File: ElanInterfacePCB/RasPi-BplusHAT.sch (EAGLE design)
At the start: 7 parts, among them J1 RASPBERRYPI-40-PIN-GPIO_PTH_N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, Q1 310mA/60V/1.6Ω, Q2 1.1A/60V/600mΩ

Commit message: PCB Work
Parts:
- removed C1: (no value), rcl:C-USC0805
- removed J1: RASPBERRYPI-40-PIN-GPIO_PTH_NO_SHROUD, SparkFun-Connectors:RASPBERRYPI-40-PIN-GPIO_PTH_NO_SHROUD
- added C2, C3: (no value), rcl:C-USC0805
- added D2, D3, D4, D5, D6: BAS40-04, diode:BAS40-04
- added K1: PIN20X2, FLYFISH:PIN20X2
- added Q10, Q12, Q4, Q6, Q8: 1.1A/60V/600mΩ, SparkFun-DiscreteSemi:MOSFET_PCH-SI2309DS
- added Q11, Q3, Q5, Q7, Q9: 310mA/60V/1.6Ω, SparkFun-DiscreteSemi:MOSFET-NCH-2N7002PW
- added R10, R12, R5, R6, R8: 1k, resistor:R-US_R0805
- added R11, R3, R4, R7, R9: 100, resistor:R-US_R0805
- added U2: MAX481CUA+, MAX481CUA_:MAX481CUA+
- R1: value (none) -> 100
- R2: value (none) -> 1k
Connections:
- new net +3V3: C3.1, K1.1, K1.17, U2.VCC
- new net +5V: K1.2, K1.4
- new net N$10: D5.C1A2, Q10.S, R9.1
- new net N$11: Q11.D, Q12.G, R12.1
- new net N$12: D6.C1A2, Q12.S, R11.1
- new net N$3: Q5.D, Q6.G, R6.1
- new net N$5: D1.C1A2, Q2.S, R4.1
- new net N$6: D3.C1A2, Q6.S, R3.1
- new net N$7: Q7.D, Q8.G, R8.1
- new net N$8: D4.C1A2, Q8.S, R7.1
- new net N$9: Q10.G, Q9.D, R10.1
- new net RXI: K1.10, U2.RO
- new net ZONE1: R1.2, R11.2, R3.2, R4.2, R7.2, R9.2
- net +12V: now also C2.1, D2.C2, D3.C2, D4.C2, D5.C2, D6.C2, Q10.D, Q12.D, Q4.D, Q6.D, Q8.D, R10.2, R12.2, R5.2, R6.2, R8.2; no longer C1.1
- net GND: now also C2.2, C3.2, D2.A1, D3.A1, D4.A1, D5.A1, D6.A1, K1.14, K1.20, K1.25, K1.30, K1.34, K1.39, K1.6, K1.9, Q11.S, Q3.S, Q5.S, Q7.S, Q9.S, U2.DE, U2.GND, U2.~RE; no longer C1.2, J1.GND@14, J1.GND@20, J1.GND@25, J1.GND@30, J1.GND@34, J1.GND@39, J1.GND@6, J1.GND@9
- net GPIO07: now also K1.26, Q1.G, Q11.G; no longer J1.CE1
- net GPIO08: now also K1.24, Q3.G; no longer J1.CE0
- net GPIO09: now also K1.21, Q5.G; no longer J1.MISO
- net GPIO10: now also K1.19, Q7.G; no longer J1.MOSI
- net GPIO11: now also K1.23, Q9.G; no longer J1.SCLK
- net N$1: now also Q3.D, Q4.G, R2.1; no longer Q1.G
- net N$2: now also D2.C1A2, Q4.S, R1.1; no longer Q1.D, Q2.G, R2.1
- net N$4: now also Q1.D, Q2.G, R5.1; no longer D1.C1A2, Q2.S, R1.1
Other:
- note added: "Checked by:"
- note added: "Drawn by:"
- note added: "FLYFISH TECHNOLOGIES d.o.o."
- note added: "Ivan Zilic"
- note added: "v0.1"
- moved on the sheet: D1, Q1, Q2, R1, R2

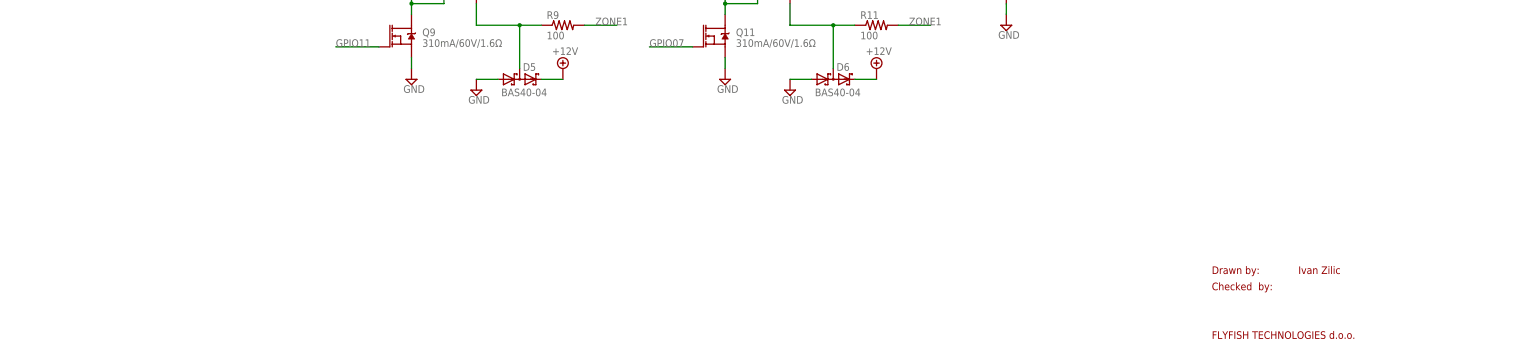
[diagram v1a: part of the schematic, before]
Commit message: Fix pin numberbing on rj45
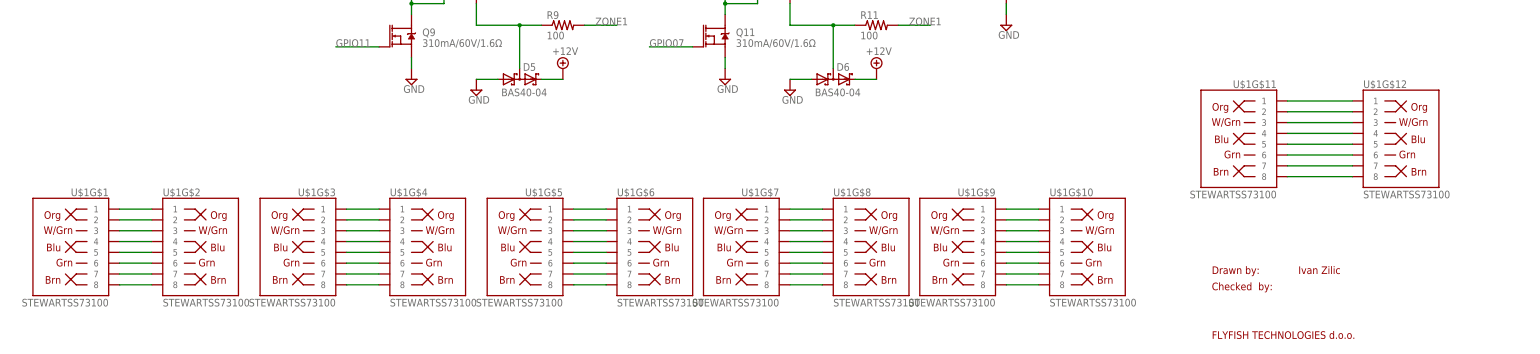
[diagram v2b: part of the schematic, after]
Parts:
- added U$1: STEWARTSS73100, Stewart_Connector_SS73100-046F:STEWARTSS73100
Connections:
- new net N$13: U$1G$1.8, U$1G$2.8
- new net N$14: U$1G$1.7, U$1G$2.7
- new net N$15: U$1G$1.6, U$1G$2.6
- new net N$16: U$1G$1.5, U$1G$2.5
- new net N$17: U$1G$1.4, U$1G$2.4
- new net N$18: U$1G$1.3, U$1G$2.3
- new net N$19: U$1G$1.2, U$1G$2.2
- new net N$20: U$1G$1.1, U$1G$2.1
- new net N$21: U$1G$3.1, U$1G$4.1
- new net N$22: U$1G$3.2, U$1G$4.2
- new net N$23: U$1G$3.3, U$1G$4.3
- new net N$24: U$1G$3.4, U$1G$4.4
- new net N$25: U$1G$3.5, U$1G$4.5
- new net N$26: U$1G$3.7, U$1G$4.7
- new net N$27: U$1G$3.6, U$1G$4.6
- new net N$28: U$1G$3.8, U$1G$4.8
- new net N$29: U$1G$5.1, U$1G$6.1
- new net N$30: U$1G$5.2, U$1G$6.2
- new net N$31: U$1G$5.3, U$1G$6.3
- new net N$32: U$1G$5.4, U$1G$6.4
- new net N$33: U$1G$5.5, U$1G$6.5
- new net N$34: U$1G$5.6, U$1G$6.6
- new net N$35: U$1G$5.7, U$1G$6.7
- new net N$36: U$1G$5.8, U$1G$6.8
- new net N$37: U$1G$7.1, U$1G$8.1
- new net N$38: U$1G$7.2, U$1G$8.2
- new net N$39: U$1G$7.3, U$1G$8.3
- new net N$40: U$1G$7.4, U$1G$8.4
- new net N$41: U$1G$7.5, U$1G$8.5
- new net N$42: U$1G$7.6, U$1G$8.6
- new net N$43: U$1G$7.7, U$1G$8.7
- new net N$44: U$1G$7.8, U$1G$8.8
- new net N$45: U$1G$10.1, U$1G$9.1
- new net N$46: U$1G$10.2, U$1G$9.2
- new net N$47: U$1G$10.3, U$1G$9.3
- new net N$48: U$1G$10.4, U$1G$9.4
- new net N$49: U$1G$10.5, U$1G$9.5
- new net N$50: U$1G$10.6, U$1G$9.6
- new net N$51: U$1G$10.7, U$1G$9.7
- new net N$52: U$1G$10.8, U$1G$9.8
- new net N$53: U$1G$11.1, U$1G$12.1
- new net N$54: U$1G$11.2, U$1G$12.2
- new net N$55: U$1G$11.3, U$1G$12.3
- new net N$56: U$1G$11.4, U$1G$12.4
- new net N$57: U$1G$11.5, U$1G$12.5
- new net N$58: U$1G$11.6, U$1G$12.6
- new net N$59: U$1G$11.7, U$1G$12.7
- new net N$60: U$1G$11.8, U$1G$12.8

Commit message: PCB Update
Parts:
- removed Q11: 310mA/60V/1.6Ω, SparkFun-DiscreteSemi:MOSFET-NCH-2N7002PW
- added C1, C4, C5, C6, C7: (no value), rcl:C-USC0805
- added JP1: (no value), pinhead:PINHD-2X4
- added Q13: 220mA/50V/3.5Ω, SparkFun-DiscreteSemi:MOSFET-NCH-BSS138
- Q1, Q3, Q5, Q7, Q9: value 310mA/60V/1.6Ω -> 220mA/50V/3.5Ω; device SparkFun-DiscreteSemi:MOSFET-NCH-2N7002PW -> SparkFun-DiscreteSemi:MOSFET-NCH-BSS138
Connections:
- removed net N$14: U$1G$1.7, U$1G$2.7
- removed net N$15 (its old number): U$1G$1.6, U$1G$2.6
- removed net N$16: U$1G$1.5, U$1G$2.5
- removed net N$17: U$1G$1.4, U$1G$2.4
- removed net N$19: U$1G$1.2, U$1G$2.2
- removed net N$22: U$1G$3.2, U$1G$4.2
- removed net N$26: U$1G$3.7, U$1G$4.7
- removed net N$27: U$1G$3.6, U$1G$4.6
- removed net N$30: U$1G$5.2, U$1G$6.2
- removed net N$34: U$1G$5.6, U$1G$6.6
- removed net N$35: U$1G$5.7, U$1G$6.7
- removed net N$38: U$1G$7.2, U$1G$8.2
- removed net N$42: U$1G$7.6, U$1G$8.6
- removed net N$43: U$1G$7.7, U$1G$8.7
- removed net N$46: U$1G$10.2, U$1G$9.2
- removed net N$50: U$1G$10.6, U$1G$9.6
- removed net N$51: U$1G$10.7, U$1G$9.7
- removed net N$54: U$1G$11.2, U$1G$12.2
- removed net N$58: U$1G$11.6, U$1G$12.6
- removed net N$59: U$1G$11.7, U$1G$12.7
- new net 485+: U$1G$1.4, U$1G$2.4, U2.A
- new net 485-: U$1G$1.5, U$1G$2.5, U2.B
- new net GPIO02: JP1.2, K1.3
- new net GPIO06: JP1.4, K1.31
- new net GPIO12: JP1.6, K1.32
- new net GPIO21: JP1.8, K1.40
- new net GPIOSEL: JP1.1, JP1.3, JP1.5, JP1.7, Q9.G
- new net ZONE2: R1.2, U$1G$3.2, U$1G$4.2
- new net ZONE3: R3.2, U$1G$5.2, U$1G$6.2
- new net ZONE4: R7.2, U$1G$7.2, U$1G$8.2
- new net ZONE5: R9.2, U$1G$10.2, U$1G$9.2
- new net ZONE6: R11.2, U$1G$11.2, U$1G$12.2
- net +12V: now also C1.1, C4.1, C5.1, C6.1, C7.1, U$1G$1.6, U$1G$10.6, U$1G$11.6, U$1G$12.6, U$1G$2.6, U$1G$3.6, U$1G$4.6, U$1G$5.6, U$1G$6.6, U$1G$7.6, U$1G$8.6, U$1G$9.6
- net +3V3: no longer K1.17
- net GND: now also C1.2, C4.2, C5.2, C6.2, C7.2, Q13.S, U$1G$1.7, U$1G$10.7, U$1G$11.7, U$1G$12.7, U$1G$2.7, U$1G$3.7, U$1G$4.7, U$1G$5.7, U$1G$6.7, U$1G$7.7, U$1G$8.7, U$1G$9.7; no longer Q11.S
- net GPIO07: now also Q13.G; no longer Q1.G, Q11.G
- net GPIO08: now also Q1.G; no longer Q3.G
- net GPIO09: now also Q3.G; no longer Q5.G
- net GPIO10: now also Q5.G; no longer Q7.G
- net GPIO11: now also Q7.G; no longer Q9.G
- net N$1: now also Q1.D; no longer Q3.D
- net N$11: now also Q9.D; no longer Q11.D
- net N$3: now also Q3.D; no longer Q5.D
- net N$4: now also Q13.D; no longer Q1.D
- net N$7: now also Q5.D; no longer Q7.D
- net N$9: now also Q7.D; no longer Q9.D
- net ZONE1: now also U$1G$1.2, U$1G$2.2; no longer R1.2, R11.2, R3.2, R7.2, R9.2
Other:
- note added: "Jeremy Rode"
- note removed: "Ivan Zilic"
- moved on the sheet: Q1, Q3, Q5, Q7, Q9, U$1G$10, U$1G$2, U$1G$3, U$1G$4, U$1G$5, U$1G$6, U$1G$7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

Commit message: Finished PCB
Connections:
- removed net +5V: K1.2, K1.4
- new net N$17: U2.DI
- net ZONE1: now also R7.2; no longer R4.2
- net ZONE2: now also R3.2; no longer R1.2
- net ZONE3: now also R9.2; no longer R3.2
- net ZONE4: now also R1.2; no longer R7.2
- net ZONE5: now also R4.2; no longer R9.2
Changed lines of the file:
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@@
 <part name="+3V1" library="supply1" library_urn="urn:adsk.eagle:library:371" deviceset="+3V3" device=""/>
 <part name="GND3" library="supply1" library_urn="urn:adsk.eagle:library:371" deviceset="GND" device=""/>
-<part name="P+1" library="supply1" library_urn="urn:adsk.eagle:library:371" deviceset="+5V" device=""/>
 <part name="Q2" library="SparkFun-DiscreteSemi" library_urn="urn:adsk.eagle:library:514" deviceset="MOSFET_PCH" device="-SI2309DS" package3d_urn="urn:adsk.eagle:package:38446/1" value="1.1A/60V/600mΩ"/>
 <part name="R4" library="resistor" library_urn="urn:adsk.eagle:library:348" deviceset="R-US_" device="R0805" package3d_urn="urn:adsk.eagle:package:26059/1" value="100"/>
@@
 <part name="SUPPLY9" library="supply2" library_urn="urn:adsk.eagle:library:372" deviceset="GND" device=""/>
 <part name="+3V2" library="supply1" library_urn="urn:adsk.eagle:library:371" deviceset="+3V3" device=""/>
-<part name="+3V3" library="supply1" library_urn="urn:adsk.eagle:library:371" deviceset="+3V3" device=""/>
 <part name="+3V4" library="supply1" library_urn="urn:adsk.eagle:library:371" deviceset="+3V3" device=""/>
 <part name="Q4" library="SparkFun-DiscreteSemi" library_urn="urn:adsk.eagle:library:514" deviceset="MOSFET_PCH" device="-SI2309DS" package3d_urn="urn:adsk.eagle:package:38446/1" value="1.1A/60V/600mΩ"/>
@@
 <part name="SUPPLY43" library="supply2" library_urn="urn:adsk.eagle:library:372" deviceset="GND" device=""/>
 <part name="SUPPLY44" library="supply2" library_urn="urn:adsk.eagle:library:372" deviceset="GND" device=""/>
-<part name="SUPPLY45" library="supply2" library_urn="urn:adsk.eagle:library:372" deviceset="+12V" device=""/>
 <part name="SUPPLY46" library="supply2" library_urn="urn:adsk.eagle:library:372" deviceset="+12V" device=""/>
 <part name="SUPPLY47" library="supply2" library_urn="urn:adsk.eagle:library:372" deviceset="+12V" device=""/>
@@
 </instance>
 <instance part="GND3" gate="1" x="40.64" y="121.92"/>
-<instance part="P+1" gate="1" x="60.96" y="182.88" smashed="yes">
-<attribute name="VALUE" x="63.5" y="185.42" size="1.778" layer="96" rot="R180"/>
-</instance>
 <instance part="Q2" gate="G$1" x="111.76" y="149.86"/>
 <instance part="R4" gate="G$1" x="134.62" y="139.7"/>
@@
 <instance part="SUPPLY9" gate="GND" x="170.18" y="200.66"/>
 <instance part="+3V2" gate="G$1" x="215.9" y="228.6" smashed="yes">
-<attribute name="VALUE" x="218.44" y="231.14" size="1.778" layer="96" rot="R180"/>
-</instance>
-<instance part="+3V3" gate="G$1" x="215.9" y="228.6" smashed="yes">
 <attribute name="VALUE" x="218.44" y="231.14" size="1.778" layer="96" rot="R180"/>
 </instance>
@@
 <instance part="SUPPLY43" gate="GND" x="259.08" y="10.16"/>
 <instance part="SUPPLY44" gate="GND" x="314.96" y="35.56"/>
-<instance part="SUPPLY45" gate="+12V" x="109.22" y="104.14"/>
 <instance part="SUPPLY46" gate="+12V" x="35.56" y="53.34"/>
 <instance part="SUPPLY47" gate="+12V" x="101.6" y="50.8"/>
@@
 <segment>
 <pinref part="+3V2" gate="G$1" pin="+3V3"/>
-<pinref part="+3V3" gate="G$1" pin="+3V3"/>
-<wire x1="215.9" y1="226.06" x2="215.9" y2="218.44" width="0.1524" layer="91"/>
-<junction x="215.9" y="226.06"/>
 <pinref part="U2" gate="A" pin="VCC"/>
-<wire x1="215.9" y1="218.44" x2="218.44" y2="218.44" width="0.1524" layer="91"/>
+<wire x1="218.44" y1="218.44" x2="215.9" y2="218.44" width="0.1524" layer="91"/>
+<wire x1="215.9" y1="218.44" x2="215.9" y2="226.06" width="0.1524" layer="91"/>
 </segment>
 <segment>
@@
 <wire x1="170.18" y1="213.36" x2="170.18" y2="220.98" width="0.1524" layer="91"/>
 <pinref part="+3V4" gate="G$1" pin="+3V3"/>
-</segment>
-</net>
-<net name="+5V" class="0">
-<segment>
-<pinref part="K1" gate="G$1" pin="2"/>
-<pinref part="P+1" gate="1" pin="+5V"/>
-<wire x1="58.42" y1="175.26" x2="60.96" y2="175.26" width="0.1524" layer="91"/>
-<wire x1="60.96" y1="175.26" x2="60.96" y2="180.34" width="0.1524" layer="91"/>
-<pinref part="K1" gate="G$1" pin="4"/>
-<wire x1="58.42" y1="172.72" x2="60.96" y2="172.72" width="0.1524" layer="91"/>
-<wire x1="60.96" y1="172.72" x2="60.96" y2="175.26" width="0.1524" layer="91"/>
-<junction x="60.96" y="175.26"/>
 </segment>
 </net>
@@
 <wire x1="116.84" y1="101.6" x2="116.84" y2="93.98" width="0.1524" layer="91"/>
 <junction x="109.22" y="101.6"/>
-<pinref part="SUPPLY45" gate="+12V" pin="+12V"/>
 </segment>
 <segment>
@@
 <net name="ZONE1" class="0">
 <segment>
-<pinref part="R4" gate="G$1" pin="2"/>
-<wire x1="139.7" y1="139.7" x2="147.32" y2="139.7" width="0.1524" layer="91"/>
-<label x="142.24" y="139.7" size="1.778" layer="95"/>
-</segment>
-<segment>
 <pinref part="U$1" gate="G$2" pin="2"/>
 <pinref part="U$1" gate="G$1" pin="2"/>
 <wire x1="50.8" y1="33.02" x2="33.02" y2="33.02" width="0.1524" layer="91"/>
 <label x="38.1" y="33.02" size="1.778" layer="95"/>
+</segment>
+<segment>
+<pinref part="R7" gate="G$1" pin="2"/>
+<wire x1="360.68" y1="137.16" x2="368.3" y2="137.16" width="0.1524" layer="91"/>
+<label x="363.22" y="137.16" size="1.778" layer="95"/>
 </segment>
 </net>
@@
 <net name="ZONE2" class="0">
 <segment>
-<pinref part="R1" gate="G$1" pin="2"/>
-<wire x1="213.36" y1="139.7" x2="220.98" y2="139.7" width="0.1524" layer="91"/>
-<label x="215.9" y="139.7" size="1.778" layer="95"/>
-</segment>
-<segment>
 <pinref part="U$1" gate="G$4" pin="2"/>
 <pinref part="U$1" gate="G$3" pin="2"/>
@@
 <label x="106.68" y="43.18" size="1.778" layer="95"/>
 </segment>
-</net>
-<net name="ZONE3" class="0">
 <segment>
 <pinref part="R3" gate="G$1" pin="2"/>
@@
 <label x="289.56" y="137.16" size="1.778" layer="95"/>
 </segment>
+</net>
+<net name="ZONE3" class="0">
 <segment>
 <pinref part="U$1" gate="G$5" pin="2"/>
@@
 <label x="160.02" y="45.72" size="1.778" layer="95"/>
 </segment>
+<segment>
+<pinref part="R9" gate="G$1" pin="2"/>
+<wire x1="142.24" y1="78.74" x2="149.86" y2="78.74" width="0.1524" layer="91"/>
+<label x="144.78" y="78.74" size="1.778" layer="95"/>
+</segment>
 </net>
 <net name="ZONE4" class="0">
-<segment>
-<pinref part="R7" gate="G$1" pin="2"/>
-<wire x1="360.68" y1="137.16" x2="368.3" y2="137.16" width="0.1524" layer="91"/>
-<label x="363.22" y="137.16" size="1.778" layer="95"/>
-</segment>
 <segment>
 <pinref part="U$1" gate="G$7" pin="2"/>
@@
 <label x="210.82" y="43.18" size="1.778" layer="95"/>
 </segment>
+<segment>
+<pinref part="R1" gate="G$1" pin="2"/>
+<wire x1="213.36" y1="139.7" x2="220.98" y2="139.7" width="0.1524" layer="91"/>
+<label x="215.9" y="139.7" size="1.778" layer="95"/>
+</segment>
 </net>
 <net name="ZONE5" class="0">
-<segment>
-<pinref part="R9" gate="G$1" pin="2"/>
-<wire x1="142.24" y1="78.74" x2="149.86" y2="78.74" width="0.1524" layer="91"/>
-<label x="144.78" y="78.74" size="1.778" layer="95"/>
-</segment>
 <segment>
 <pinref part="U$1" gate="G$10" pin="2"/>
@@
 <wire x1="259.08" y1="43.18" x2="271.78" y2="43.18" width="0.1524" layer="91"/>
 <label x="261.62" y="43.18" size="1.778" layer="95"/>
+</segment>
+<segment>
+<pinref part="R4" gate="G$1" pin="2"/>
+<wire x1="139.7" y1="139.7" x2="147.32" y2="139.7" width="0.1524" layer="91"/>
+<label x="142.24" y="139.7" size="1.778" layer="95"/>
 </segment>
 </net>
@@
 </segment>
 </net>
+<net name="N$17" class="0">
+<segment>
+<pinref part="U2" gate="A" pin="DI"/>
+<junction x="218.44" y="205.74"/>
+</segment>
+</net>
 </nets>
 </sheet>
 </sheets>
+<errors>
+</errors>
 </schematic>
 </drawing>

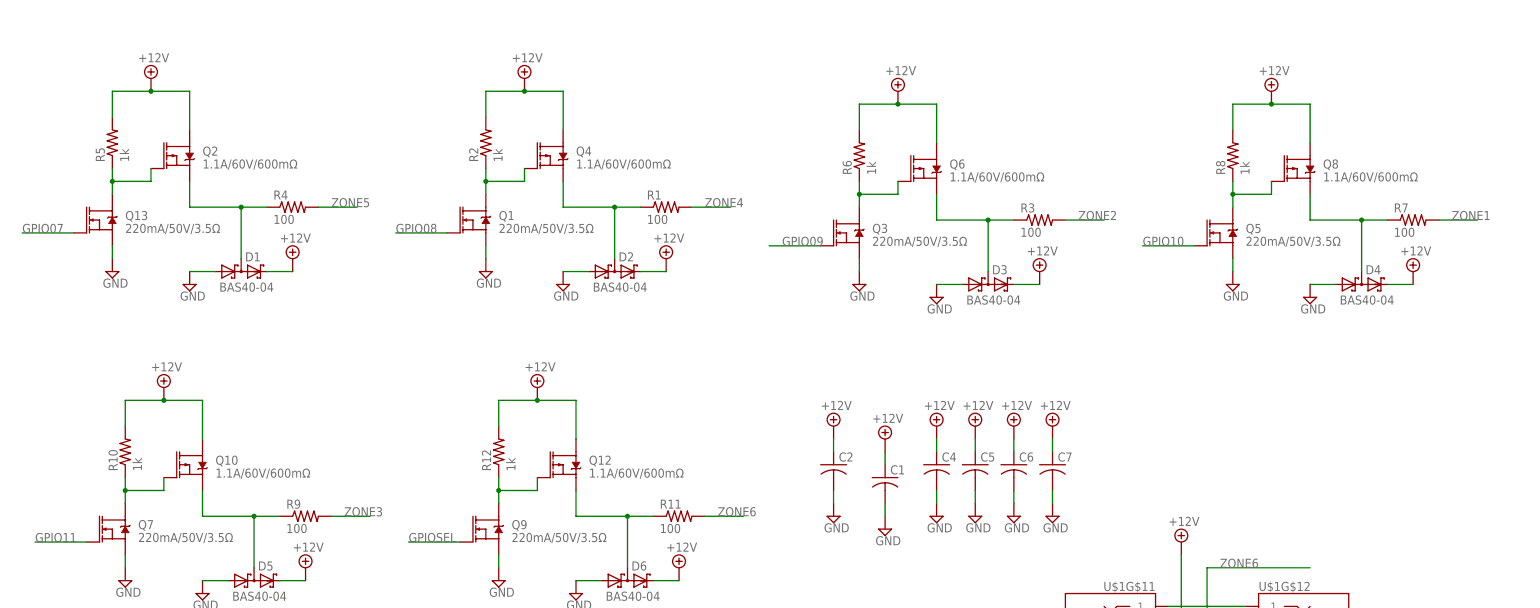
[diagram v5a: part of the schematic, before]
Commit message: Fixed inverted PMOS in schematic
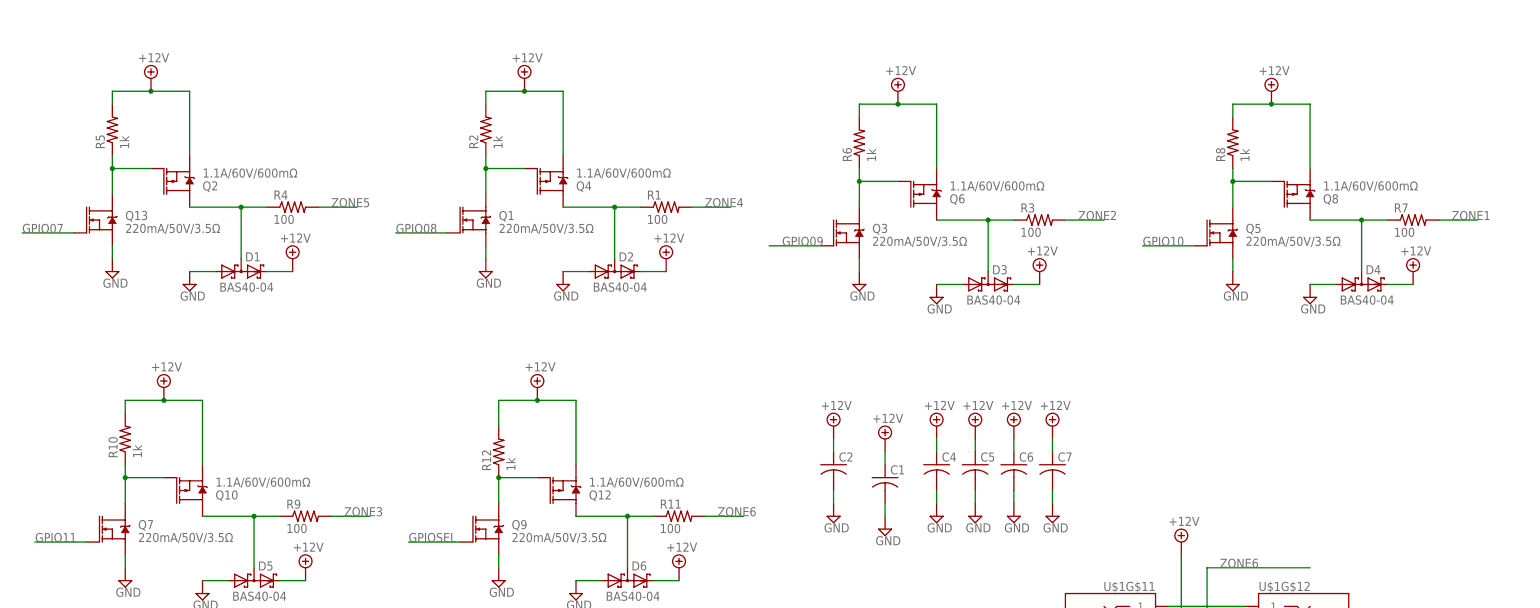
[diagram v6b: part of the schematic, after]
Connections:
- net +12V: now also Q10.S, Q12.S, Q2.S, Q4.S, Q6.S, Q8.S; no longer Q10.D, Q12.D, Q2.D, Q4.D, Q6.D, Q8.D
- net N$10: now also Q10.D; no longer Q10.S
- net N$12: now also Q12.D; no longer Q12.S
- net N$2: now also Q4.D; no longer Q4.S
- net N$5: now also Q2.D; no longer Q2.S
- net N$6: now also Q6.D; no longer Q6.S
- net N$8: now also Q8.D; no longer Q8.S
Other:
- moved on the sheet: Q10, Q12, Q2, Q4, Q6, Q8, R10, R2, R5, R6, R8
